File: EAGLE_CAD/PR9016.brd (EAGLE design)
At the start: 70 x 70 mm, 73 parts, among them J1 M3_SCREW_POST, SW1 C&K_PTS645

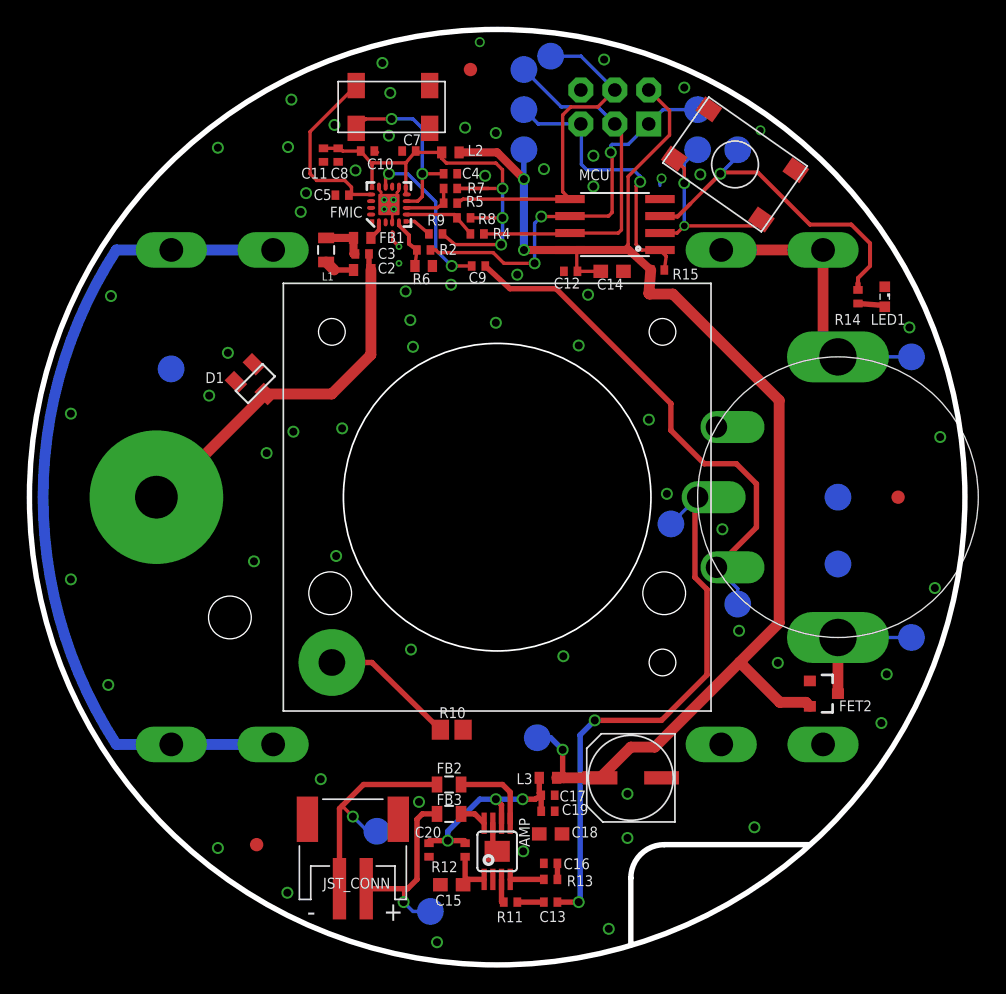
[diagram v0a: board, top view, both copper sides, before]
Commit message: 0402 packages, minor re-routing
and incremented the version to pr9016
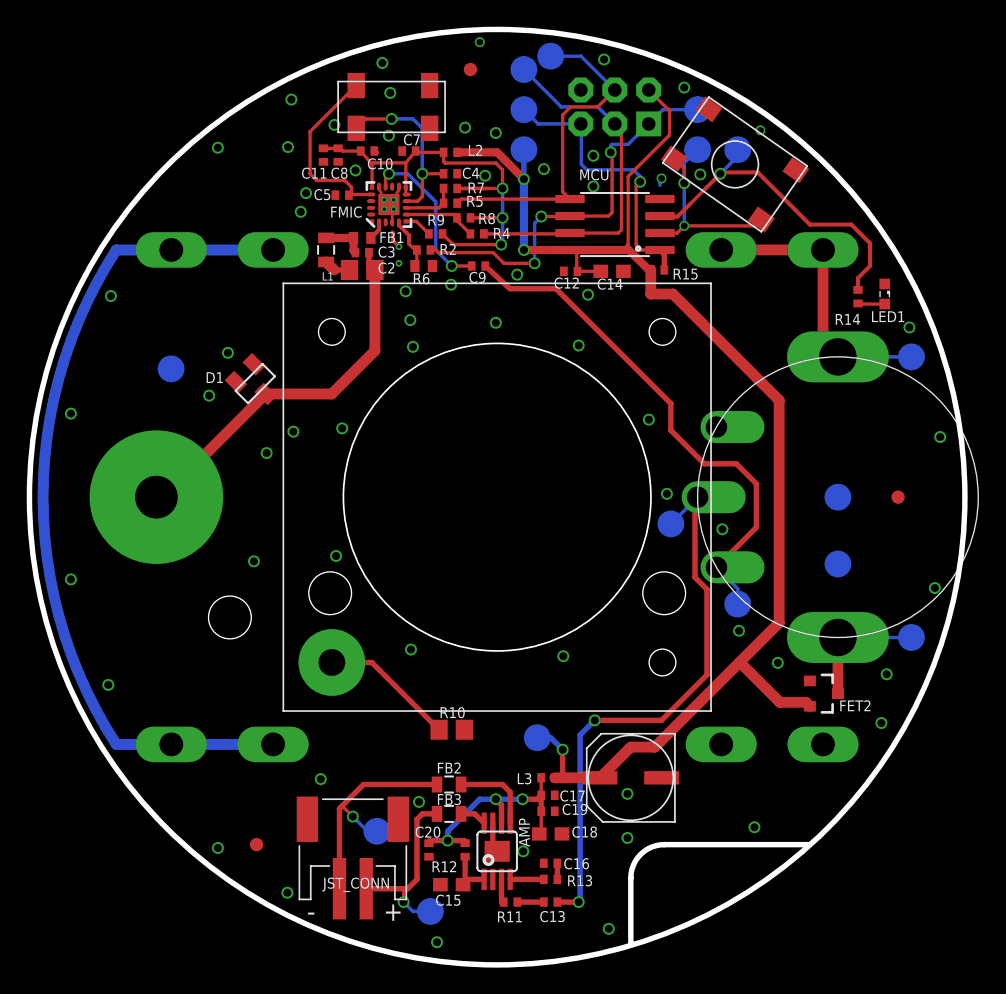
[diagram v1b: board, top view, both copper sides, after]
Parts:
- C2: device resistor:C0402 -> resistor:C0805
- L2, L3: device SparkFun-Passives:C0402 -> PR_Parts_Library:C0402_WORTHINGTON
- moved LED1 0.20 mm to (64.0, 50.2)
- moved C3 0.10 mm to (24.9, 53.3)
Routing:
- net N$18: track 16.3 -> 18.1 mm
- net ANT: track 28.2 -> 28.7 mm

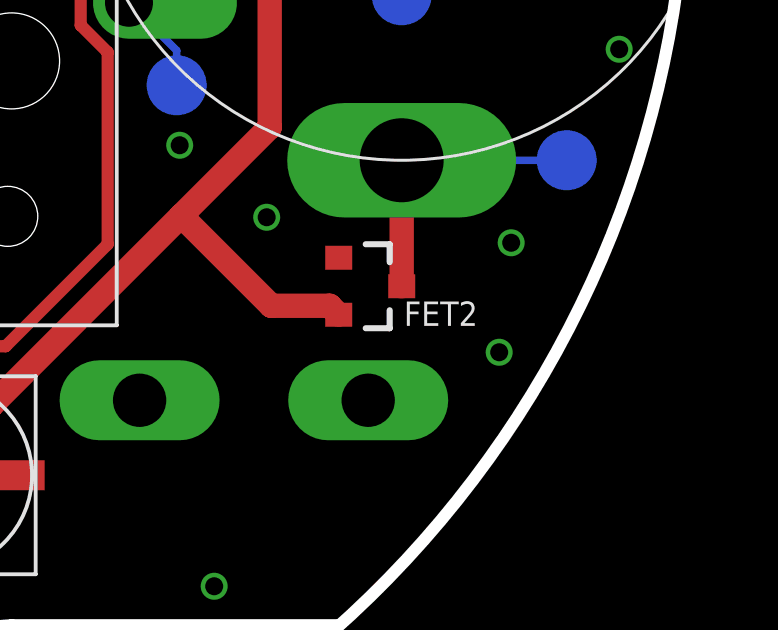
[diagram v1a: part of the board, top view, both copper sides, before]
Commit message: updated part names per WAi feedback
changed the fiducials to MARK1, etc
changed “J1” to “ANT_MOUNT”, “FET2” to “FET1”, “U$1” to “SPKR_PLACE”,
and “U$6” to “Y1”
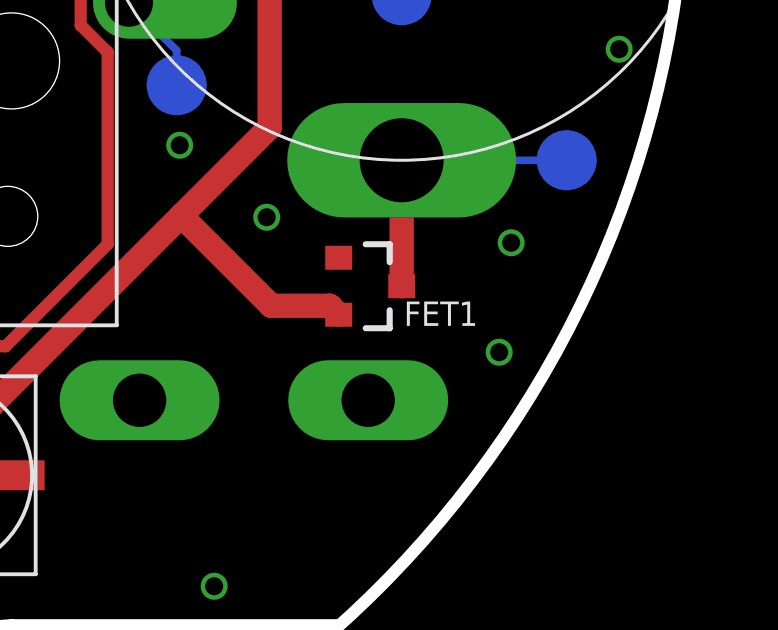
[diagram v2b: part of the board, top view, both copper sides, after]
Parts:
- renumbered FET2 to FET1, J1 to ANT_MOUNT, U$1 to SPKR_PLACE, U$3 to MARK1, U$4 to MARK2, U$5 to MARK3, U$6 to Y1
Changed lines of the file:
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@@
 <attribute name="VALUE" x="34.632" y="7.711" size="1.27" layer="27" rot="R90"/>
 </element>
-<element name="J1" library="PR_Parts_Library" package="M3_SCREW_POST" value="M3_SCREW_POST" x="9.5" y="35" locked="yes" smashed="yes"/>
+<element name="ANT_MOUNT" library="PR_Parts_Library" package="M3_SCREW_POST" value="M3_SCREW_POST" x="9.5" y="35" locked="yes" smashed="yes"/>
 <element name="R1" library="PR_Parts_Library" package="RV170SF_TAIWANA_POT_SW" value="RV170SF_TAIWANA_POT_SW" x="60.5" y="35" locked="yes" rot="R270"/>
 <element name="MCU" library="SparkFun-DigitalIC" package="SO08-EIAJ" value="Tiny45-20-SMT" x="43.8" y="55.4" smashed="yes" rot="R90">
@@
 <attribute name="VALUE" x="39.508" y="67.238" size="0.254" layer="28" rot="MR0"/>
 </element>
-<element name="U$3" library="adafruit" package="FIDUCIAL_1MM" value="FIDUCIAL" x="17" y="9"/>
-<element name="U$4" library="adafruit" package="FIDUCIAL_1MM" value="FIDUCIAL" x="33" y="67"/>
-<element name="U$5" library="adafruit" package="FIDUCIAL_1MM" value="FIDUCIAL" x="65" y="35"/>
-<element name="U$6" library="PR_Parts_Library" package="ABS25XTAL" value="ABS25XTAL" x="27.2" y="64.2"/>
+<element name="MARK1" library="adafruit" package="FIDUCIAL_1MM" value="FIDUCIAL" x="17" y="9"/>
+<element name="MARK2" library="adafruit" package="FIDUCIAL_1MM" value="FIDUCIAL" x="33" y="67"/>
+<element name="MARK3" library="adafruit" package="FIDUCIAL_1MM" value="FIDUCIAL" x="65" y="35"/>
+<element name="Y1" library="PR_Parts_Library" package="ABS25XTAL" value="ABS25XTAL" x="27.2" y="64.2"/>
 <element name="C18" library="resistor" package="C0603" value="10uF" x="39" y="9.8" smashed="yes" rot="R180">
 <attribute name="NAME" x="40.565" y="9.535" size="0.8128" layer="25" font="vector" ratio="16"/>
@@
 <attribute name="VALUE" x="32.965" y="50.395" size="1.27" layer="27"/>
 </element>
-<element name="FET2" library="PR_Parts_Library" package="AO3435" value="AO3435" x="59.4" y="20.3" smashed="yes" rot="R270">
+<element name="FET1" library="PR_Parts_Library" package="AO3435" value="AO3435" x="59.4" y="20.3" smashed="yes" rot="R270">
 <attribute name="NAME" x="60.5745" y="18.978" size="0.8128" layer="25" font="vector" ratio="16"/>
 <attribute name="VALUE" x="59.2095" y="21.316" size="0.4064" layer="27" rot="R270"/>
 </element>
-<element name="U$1" library="PR_Parts_Library" package="CE32A_FOR_JST" value="" x="35" y="35" locked="yes"/>
+<element name="SPKR_PLACE" library="PR_Parts_Library" package="CE32A_FOR_JST" value="" x="35" y="35" locked="yes"/>
 <element name="TP14" library="testpad" package="TP20R" value="TPTP20R" x="66" y="24.5" smashed="yes" rot="MR0">
 <attribute name="TP_SIGNAL_NAME" value="" x="66" y="21.96" size="1" layer="38" rot="MR0"/>
@@
 <via x="47.7" y="35.25" extent="1-16" drill="0.6"/>
 <via x="20.7" y="57.75" extent="1-16" drill="0.6"/>
-<contactref element="FET2" pad="1"/>
+<contactref element="FET1" pad="1"/>
 <via x="26.55" y="56.55" extent="1-16" drill="0.254"/>
 <via x="27.25" y="57.25" extent="1-16" drill="0.254"/>
@@
 <signal name="N$1">
 <contactref element="FMIC" pad="9"/>
-<contactref element="U$6" pad="P$1"/>
+<contactref element="Y1" pad="P$1"/>
 <contactref element="C4" pad="1"/>
 <wire x1="30.9929" y1="59.2" x2="29.4" y2="59.2" width="0.254" layer="1"/>
@@
 <wire x1="56.1" y1="42.25" x2="48.15" y2="50.2" width="0.8128" layer="1"/>
 <wire x1="56.15" y1="19.65" x2="53.15" y2="22.65" width="0.8128" layer="1"/>
-<contactref element="FET2" pad="2"/>
+<contactref element="FET1" pad="2"/>
 <wire x1="56.15" y1="19.65" x2="58.1" y2="19.65" width="0.8128" layer="1"/>
 <wire x1="58.1" y1="19.65" x2="58.4" y2="19.35" width="0.8128" layer="1"/>
@@
 <signal name="SW_IN">
 <contactref element="R1" pad="SW_IN"/>
-<contactref element="FET2" pad="3"/>
+<contactref element="FET1" pad="3"/>
 <wire x1="60.5" y1="20.3" x2="60.5" y2="24.5" width="0.8128" layer="1"/>
 <contactref element="TP14" pad="TP"/>
@@
 </signal>
 <signal name="ANT" class="1">
-<contactref element="J1" pad="P$1"/>
+<contactref element="ANT_MOUNT" pad="P$1"/>
 <contactref element="D1" pad="3"/>
 <contactref element="C2" pad="1"/>
@@
 </signal>
 <signal name="N$8">
-<contactref element="U$1" pad="LID_GND"/>
+<contactref element="SPKR_PLACE" pad="LID_GND"/>
 <contactref element="R10" pad="2"/>
 <wire x1="30.65" y1="17.6" x2="25.6198" y2="22.6302" width="0.4064" layer="1"/>
@@
 <signal name="N$10">
 <contactref element="FMIC" pad="17"/>
-<contactref element="U$6" pad="P$4"/>
+<contactref element="Y1" pad="P$4"/>
 <contactref element="C5" pad="1"/>
 <wire x1="25.565" y1="57.65" x2="24.1" y2="57.65" width="0.254" layer="1"/>
